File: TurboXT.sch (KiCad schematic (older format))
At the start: 20 parts, among them J1 8284 Socket, J2 HRQDMA, J3 DMAWAIT, J4 VCC, J5 GND, J6 Turbo LED, SW1 TURBO SWITCH, U1 8284, U2 74LS92, U3 74LS74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

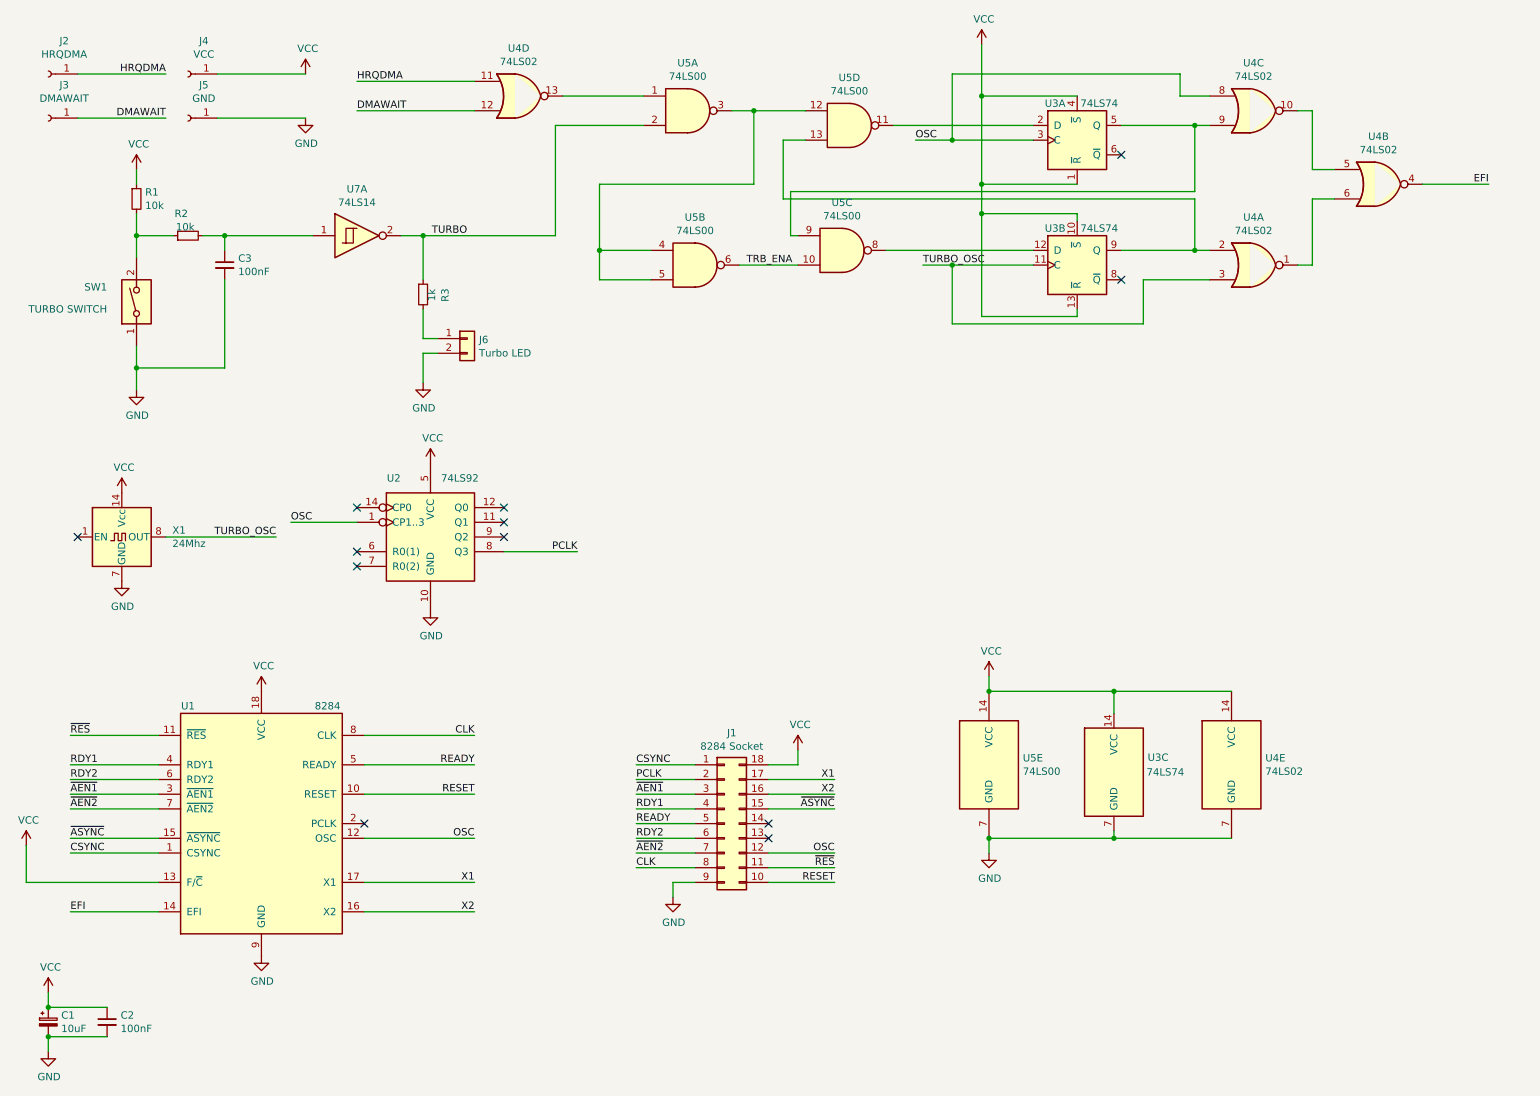
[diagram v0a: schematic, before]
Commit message: Drawn the schematic
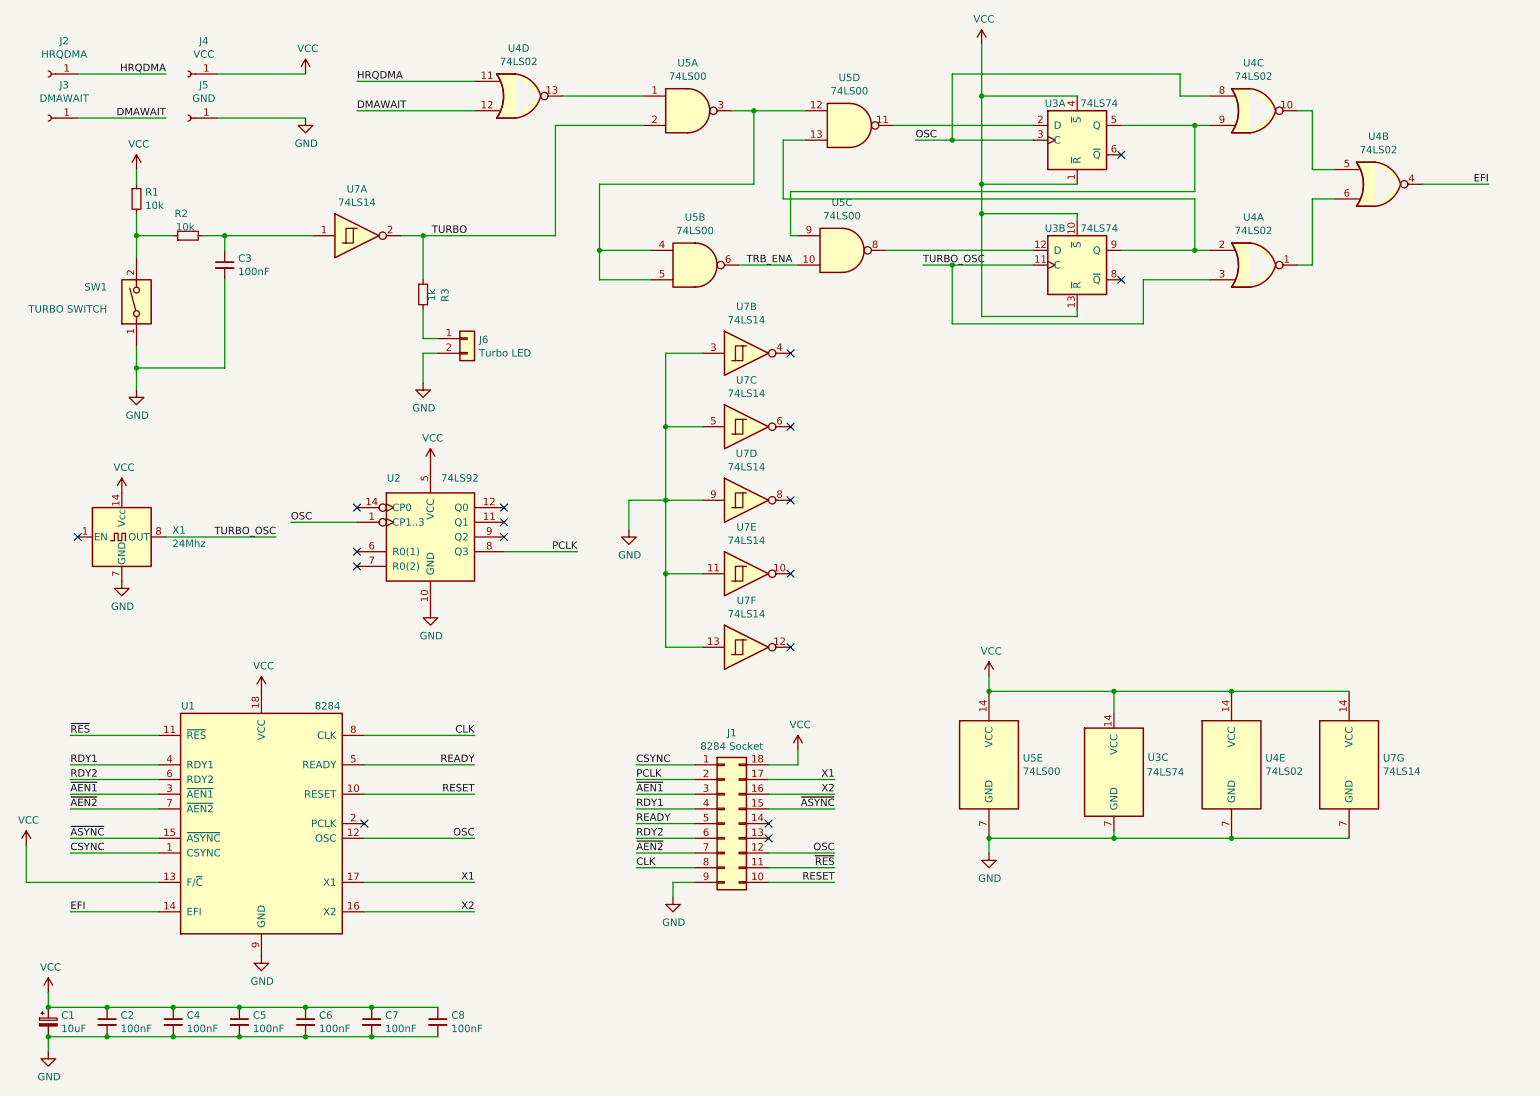
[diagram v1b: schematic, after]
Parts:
- added C4, C5, C6, C7, C8: 100nF, Capacitor_THT:C_Disc_D6.0mm_W2.5mm_P5.00mm, symbol Device:C_Small
- added unit 7 of U7
- added unit 2 of U7
- added unit 3 of U7
- added unit 4 of U7
- added unit 5 of U7
- added unit 6 of U7
- J1: footprint (none) -> Package_DIP:DIP-18_W7.62mm_LongPads
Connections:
- net GND: now also C4.2, C5.2, C6.2, C7.2, C8.2, U7.11, U7.13, U7.3, U7.5, U7.7 (GND), U7.9
- net VCC: now also C4.1, C5.1, C6.1, C7.1, C8.1, U7.14 (VCC)
- no-connect marks 12 -> 17

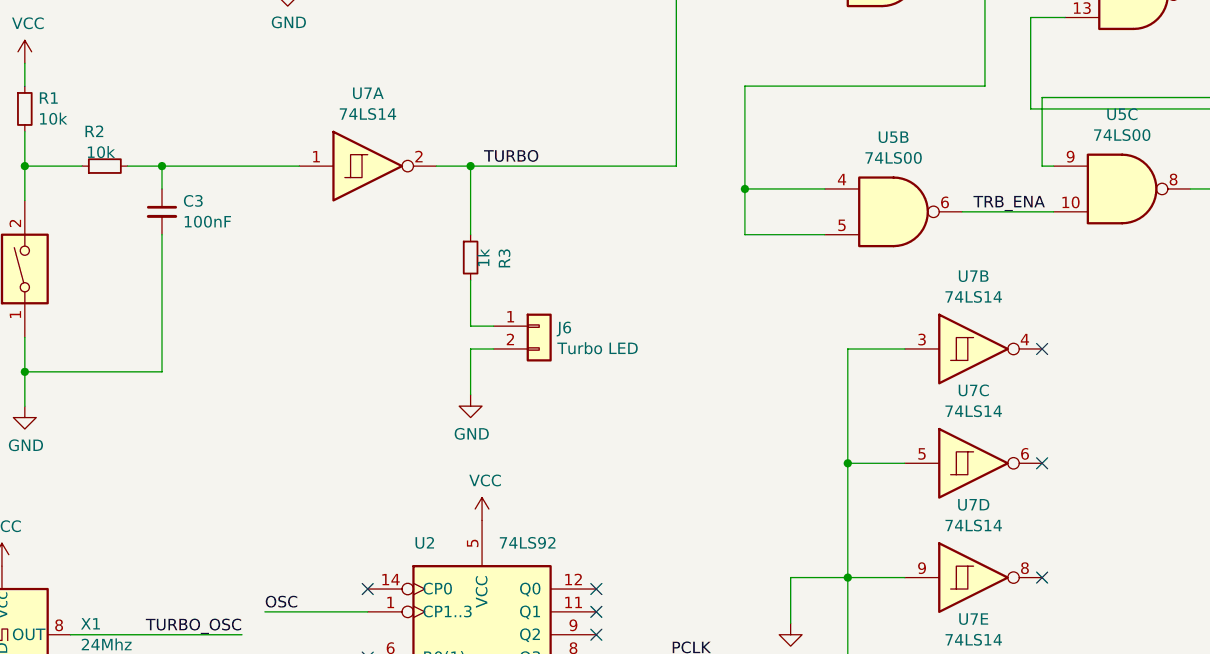
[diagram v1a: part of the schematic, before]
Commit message: Change connection for led
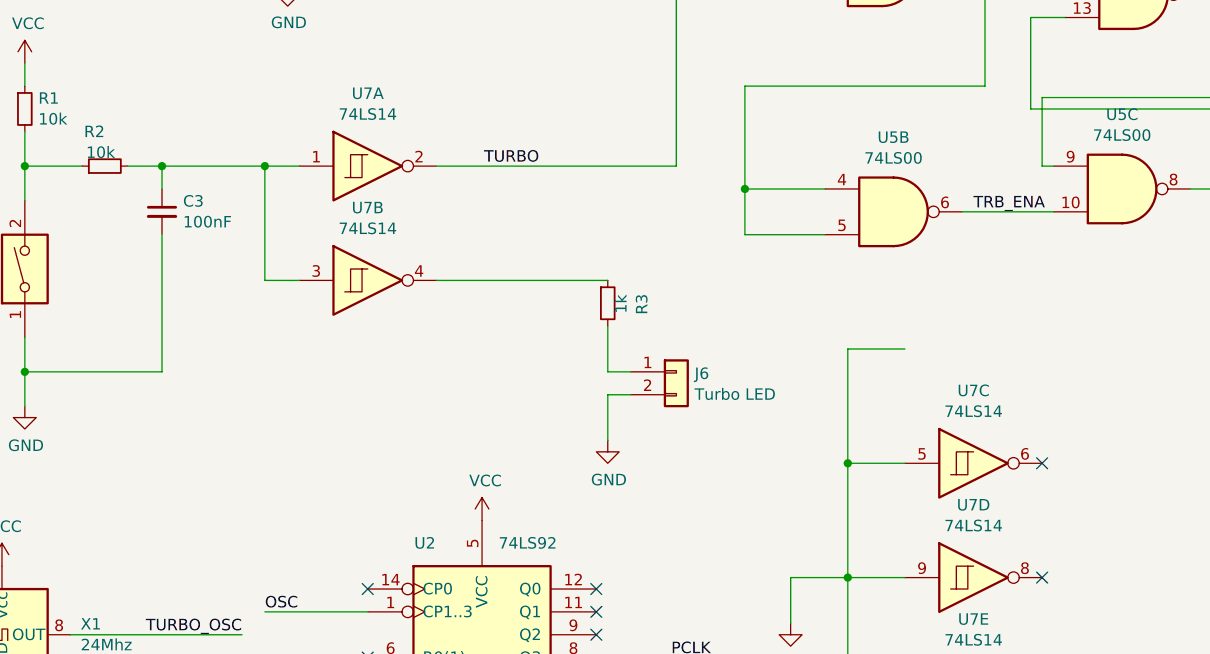
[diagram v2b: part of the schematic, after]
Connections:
- net GND: no longer U7.3
- net TURBO: no longer R3.1
- net at C3.1, R2.2, U7.1: now also U7.3
- net at U7.4: now also R3.1
- no-connect marks 17 -> 16
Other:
- moved on the sheet: J6, R3, U7B
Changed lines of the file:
@@
 $EndComp
 Wire Wire Line
-	2650 2000 2050 2000
+	2650 2000 2500 2000
 Connection ~ 2050 2000
 Text Label 3700 2000 2    50   ~ 0
@@
 Wire Wire Line
 	4300 1250 4900 1250
-Wire Wire Line
-	3250 2000 3400 2000
 $Comp
 L 74xx:74LS00 U5
@@
 L Device:R_Small R3
 U 1 1 6060A70E
-P 3400 2400
-F 0 "R3" V 3550 2350 50  0000 L CNN
-F 1 "1k" V 3459 2355 50  0000 L CNN
-F 2 "Resistor_THT:R_Axial_DIN0207_L6.3mm_D2.5mm_P10.16mm_Horizontal" H 3400 2400 50  0001 C CNN
-F 3 "~" H 3400 2400 50  0001 C CNN
-	1    3400 2400
-	1    0    0    -1
-$EndComp
-Wire Wire Line
-	3400 2300 3400 2000
-Connection ~ 3400 2000
-Wire Wire Line
-	3400 2000 4300 2000
+P 4000 2600
+F 0 "R3" V 4150 2550 50  0000 L CNN
+F 1 "1k" V 4059 2555 50  0000 L CNN
+F 2 "Resistor_THT:R_Axial_DIN0207_L6.3mm_D2.5mm_P10.16mm_Horizontal" H 4000 2600 50  0001 C CNN
+F 3 "~" H 4000 2600 50  0001 C CNN
+	1    4000 2600
+	1    0    0    -1
+$EndComp
 $Comp
 L power:GND #PWR0119
 U 1 1 60621A7F
-P 3400 3000
-F 0 "#PWR0119" H 3400 2750 50  0001 C CNN
-F 1 "GND" H 3405 2827 50  0000 C CNN
-F 2 "" H 3400 3000 50  0001 C CNN
-F 3 "" H 3400 3000 50  0001 C CNN
-	1    3400 3000
+P 4000 3200
+F 0 "#PWR0119" H 4000 2950 50  0001 C CNN
+F 1 "GND" H 4005 3027 50  0000 C CNN
+F 2 "" H 4000 3200 50  0001 C CNN
+F 3 "" H 4000 3200 50  0001 C CNN
+	1    4000 3200
 	1    0    0    -1
 $EndComp
@@
 L Connector_Generic:Conn_01x02 J6
 U 1 1 606252CB
-P 3700 2700
-F 0 "J6" H 3780 2692 50  0000 L CNN
-F 1 "Turbo LED" H 3780 2601 50  0000 L CNN
-F 2 "Connector_PinHeader_2.54mm:PinHeader_1x02_P2.54mm_Vertical" H 3700 2700 50  0001 C CNN
-F 3 "~" H 3700 2700 50  0001 C CNN
-	1    3700 2700
-	1    0    0    -1
-$EndComp
-Wire Wire Line
-	3400 2500 3400 2700
-Wire Wire Line
-	3400 2700 3500 2700
-Wire Wire Line
-	3400 3000 3400 2800
-Wire Wire Line
-	3400 2800 3500 2800
+P 4300 2900
+F 0 "J6" H 4380 2892 50  0000 L CNN
+F 1 "Turbo LED" H 4380 2801 50  0000 L CNN
+F 2 "Connector_PinHeader_2.54mm:PinHeader_1x02_P2.54mm_Vertical" H 4300 2900 50  0001 C CNN
+F 3 "~" H 4300 2900 50  0001 C CNN
+	1    4300 2900
+	1    0    0    -1
+$EndComp
+Wire Wire Line
+	4000 2700 4000 2900
+Wire Wire Line
+	4000 2900 4100 2900
+Wire Wire Line
+	4000 3200 4000 3000
+Wire Wire Line
+	4000 3000 4100 3000
 $Comp
 L 74xx:74LS14 U7
@@
 L 74xx:74LS14 U7
 U 2 1 60695CC6
-P 5600 2800
-F 0 "U7" H 5600 3117 50  0000 C CNN
-F 1 "74LS14" H 5600 3026 50  0000 C CNN
-F 2 "Package_DIP:DIP-14_W7.62mm_LongPads" H 5600 2800 50  0001 C CNN
-F 3 "http://www.ti.com/lit/gpn/sn74LS14" H 5600 2800 50  0001 C CNN
-	2    5600 2800
+P 2950 2500
+F 0 "U7" H 2950 2817 50  0000 C CNN
+F 1 "74LS14" H 2950 2726 50  0000 C CNN
+F 2 "Package_DIP:DIP-14_W7.62mm_LongPads" H 2950 2500 50  0001 C CNN
+F 3 "http://www.ti.com/lit/gpn/sn74LS14" H 2950 2500 50  0001 C CNN
+	2    2950 2500
 	1    0    0    -1
 $EndComp
@@
 	1    0    0    -1
 $EndComp
-NoConn ~ 5900 2800
 NoConn ~ 5900 3300
 NoConn ~ 5900 3800
@@
 Connection ~ 1700 7450
 Connection ~ 1250 7450
+Wire Wire Line
+	2500 2000 2500 2500
+Wire Wire Line
+	2500 2500 2650 2500
+Connection ~ 2500 2000
+Wire Wire Line
+	2500 2000 2050 2000
+Wire Wire Line
+	3250 2000 4300 2000
+Wire Wire Line
+	3250 2500 4000 2500
 $EndSCHEMATC

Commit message: Fix schematics
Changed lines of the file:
@@
 NoConn ~ 5900 4800
-Wire Wire Line
-	5300 2800 5050 2800
-Wire Wire Line
-	5050 2800 5050 3300
 Wire Wire Line
 	5050 4800 5300 4800
@@
 Wire Wire Line
 	5300 3300 5050 3300
-Connection ~ 5050 3300
 Wire Wire Line
 	5050 3300 5050 3800

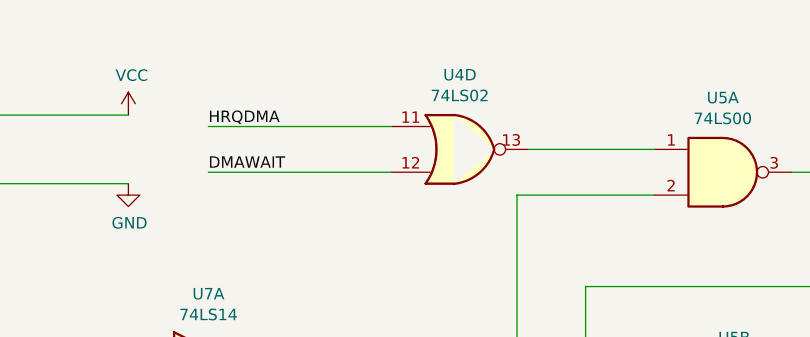
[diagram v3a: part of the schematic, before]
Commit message: Add notes to PCB and changed silkscreen
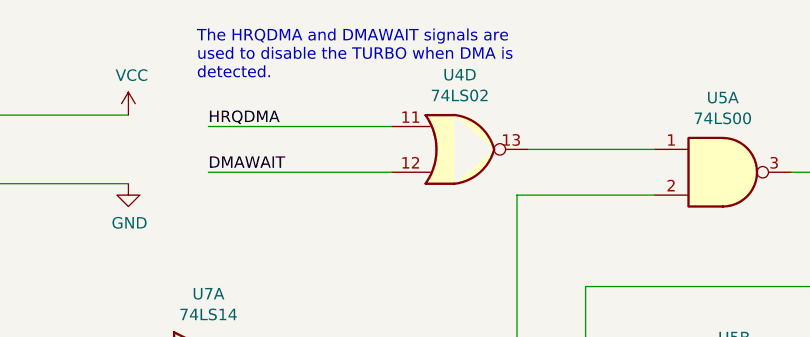
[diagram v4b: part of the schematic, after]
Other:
- note added: "The HRQDMA and DMAWAIT signals are\nused to disable the TURBO when DMA is\ndetected."
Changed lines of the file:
@@
 Wire Wire Line
 	3250 2500 4000 2500
+Text Notes 2900 750  0    50   ~ 0
+The HRQDMA and DMAWAIT signals are\nused to disable the TURBO when DMA is\ndetected.
 $EndSCHEMATC

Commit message: More notes in schematics
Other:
- note added: "- HRQDMA -> Pin 10 of U28 (8237 DMA)\n- DMAWAIT -> Pin 7 of U88 (74LS175)"
- note added: "This board will generate a clock at 1/3\nof X1's frequency.\n\nIf the DMAWAIT and the HRQDMA signals\nare connected, they will be used to disable\nthe TURBO and revert to original clock\nwhile DMA is in progress.\n\nInstalling an 24Mhz oscillator will provide an\n8Mhz clock."
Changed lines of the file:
@@
 Title "TurboXT"
 Date ""
-Rev "0.1"
+Rev "1.1"
 Comp ""
 Comment1 "Copyright (c) 2014 Sergey Kiselev"
@@
 Text Notes 2900 750  0    50   ~ 0
 The HRQDMA and DMAWAIT signals are\nused to disable the TURBO when DMA is\ndetected.
+Text Notes 6500 4400 0    100  ~ 0
+This board will generate a clock at 1/3\nof  X1's frequency.\n\nIf the DMAWAIT and the HRQDMA signals\nare connected, they will be used to disable\nthe TURBO and revert to original clock\nwhile DMA is in progress.\n\nInstalling an 24Mhz oscillator will provide an\n8Mhz clock.
+Text Notes 2050 1600 0    50   ~ 0
+- HRQDMA -> Pin 10 of U28 (8237 DMA)\n- DMAWAIT -> Pin 7 of U88 (74LS175)
 $EndSCHEMATC

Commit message: Add notes
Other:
- note added: "Please note that some 8284 (CMOS?) do not drive the\nOSC output when F/C signal is high.\nThe real 8284 drives OSC always from the crystal input\nfrequency regardless of the F/C signal state."
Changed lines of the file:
@@
 Text Notes 2050 1600 0    50   ~ 0
 - HRQDMA -> Pin 10 of U28 (8237 DMA)\n- DMAWAIT -> Pin 7 of U88 (74LS175)
+Text Notes 4050 7300 0    50   ~ 0
+Please note that some 8284 (CMOS?) do not drive the\nOSC output when F/C signal is high.\nThe real 8284 drives OSC always from the crystal input\nfrequency regardless of the F/C signal state.
 $EndSCHEMATC

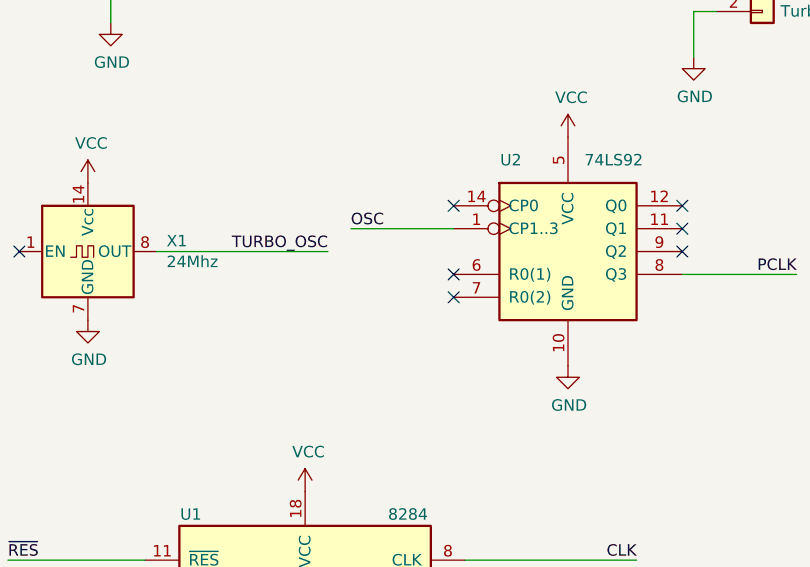
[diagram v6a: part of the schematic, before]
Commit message: Connect reset of 74LS92
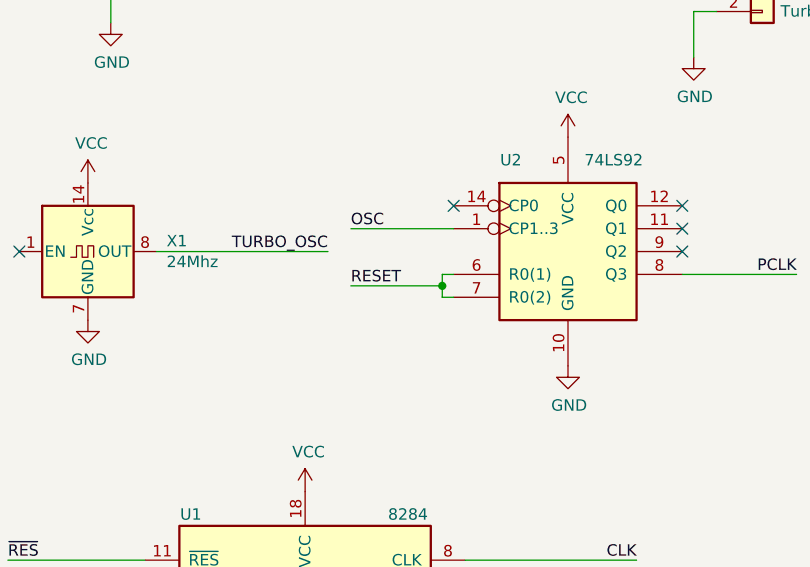
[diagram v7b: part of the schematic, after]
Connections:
- net RESET: now also U2.6 (R0(1)), U2.7 (R0(2))
- no-connect marks 16 -> 14
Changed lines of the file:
@@
 	2950 3950 2500 3950
 NoConn ~ 2950 3850
-NoConn ~ 2950 4250
-NoConn ~ 2950 4150
 NoConn ~ 3950 4050
 NoConn ~ 3950 3950
@@
 Text Notes 4050 7300 0    50   ~ 0
 Please note that some 8284 (CMOS?) do not drive the\nOSC output when F/C signal is high.\nThe real 8284 drives OSC always from the crystal input\nfrequency regardless of the F/C signal state.
+Wire Wire Line
+	2950 4150 2900 4150
+Wire Wire Line
+	2900 4150 2900 4200
+Wire Wire Line
+	2900 4250 2950 4250
+Wire Wire Line
+	2900 4200 2500 4200
+Connection ~ 2900 4200
+Wire Wire Line
+	2900 4200 2900 4250
+Text Label 2500 4200 0    50   ~ 0
+RESET
 $EndSCHEMATC

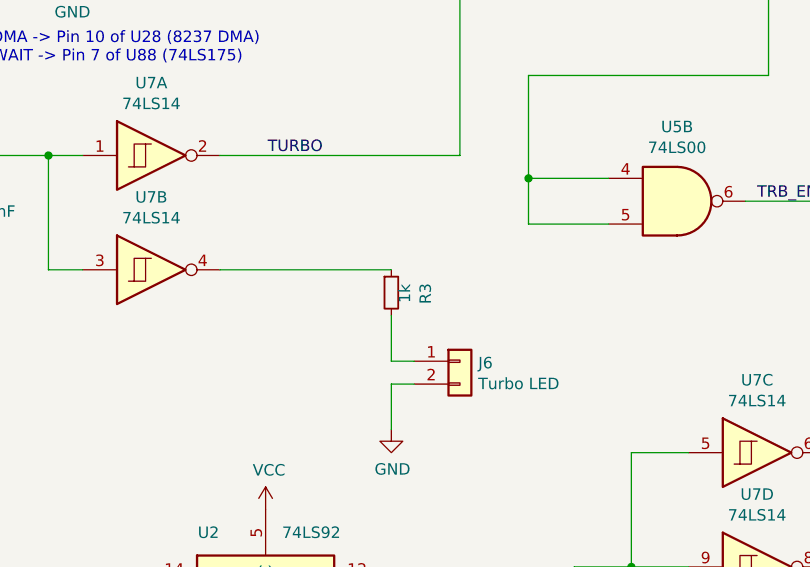
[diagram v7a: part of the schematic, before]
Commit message: Change led value and silkscreen
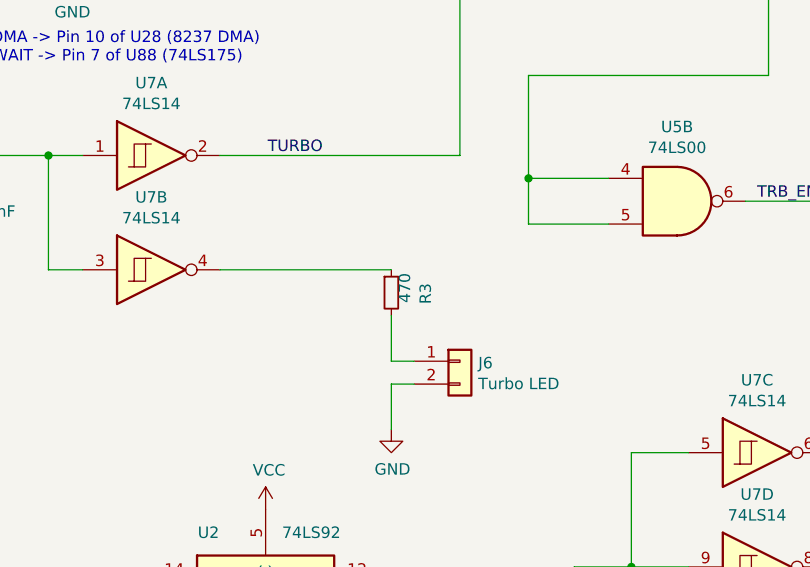
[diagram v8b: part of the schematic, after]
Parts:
- R3: value 1k -> 470
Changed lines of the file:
@@
 P 4000 2600
 F 0 "R3" V 4150 2550 50  0000 L CNN
-F 1 "1k" V 4059 2555 50  0000 L CNN
+F 1 "470" V 4059 2555 50  0000 L CNN
 F 2 "Resistor_THT:R_Axial_DIN0207_L6.3mm_D2.5mm_P10.16mm_Horizontal" H 4000 2600 50  0001 C CNN
 F 3 "~" H 4000 2600 50  0001 C CNN
